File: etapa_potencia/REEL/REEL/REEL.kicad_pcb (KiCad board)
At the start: 2 copper layers, 30 parts, among them J1 USB_B_Mini, SW1 SW_Push, SW2 SW_Reed, SW3 SW_Push, U1 Tp5400, U2 ESP32-WROOM-32, U3 FT232, U4 AMS1117-3.3

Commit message: Adición etapa de audio
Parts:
- D3: value SMBJ5383B -> DIOM4336X265N
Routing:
- net GND: track 0.00 -> 295.5 mm
- net +5V: track 0.00 -> 166.8 mm
- net Net-(D1-Pad2): track 0.00 -> 107.7 mm, vias 0 -> 2
- net /RESET: track 0.00 -> 98.7 mm, vias 0 -> 2
- net Net-(R7-Pad1): track 0.00 -> 97.5 mm, vias 0 -> 1
- net /GPIO0: track 0.00 -> 85.4 mm, vias 0 -> 2
- net Net-(D1-Pad1): track 0.00 -> 85.1 mm, vias 0 -> 2
- net +3V3: track 0.00 -> 84.8 mm, vias 0 -> 2
- net Net-(SW2-Pad2): track 0.00 -> 69.8 mm, vias 0 -> 1
- net Net-(D2-Pad1): track 0.00 -> 22.7 mm
- net Net-(R5-Pad1): track 0.00 -> 17.8 mm, vias 0 -> 2

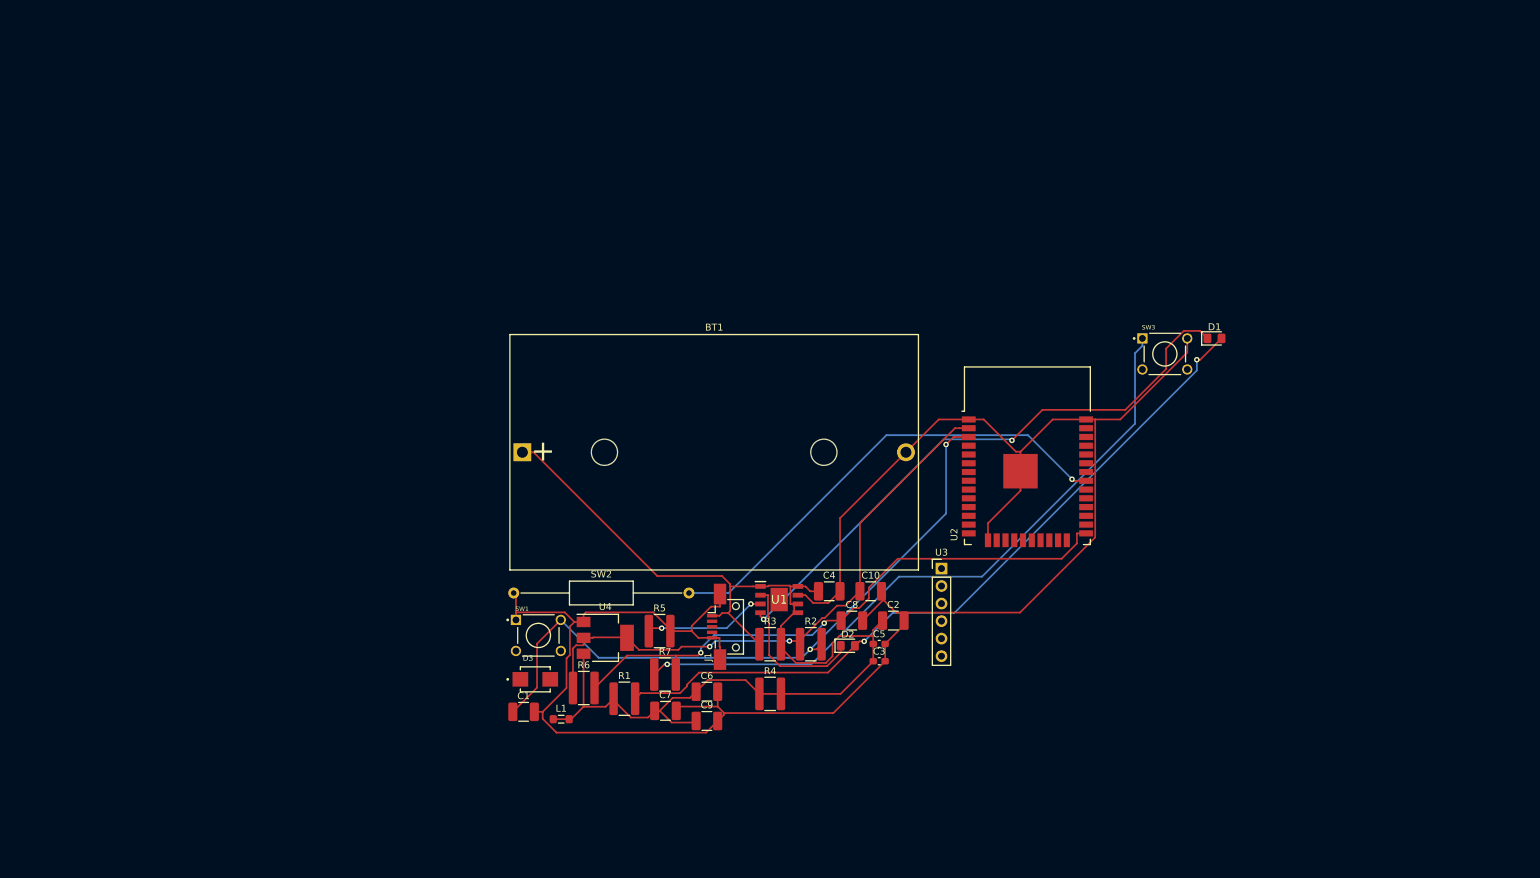
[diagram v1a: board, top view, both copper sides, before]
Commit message: Conexiones corregidas, PCB ordenada
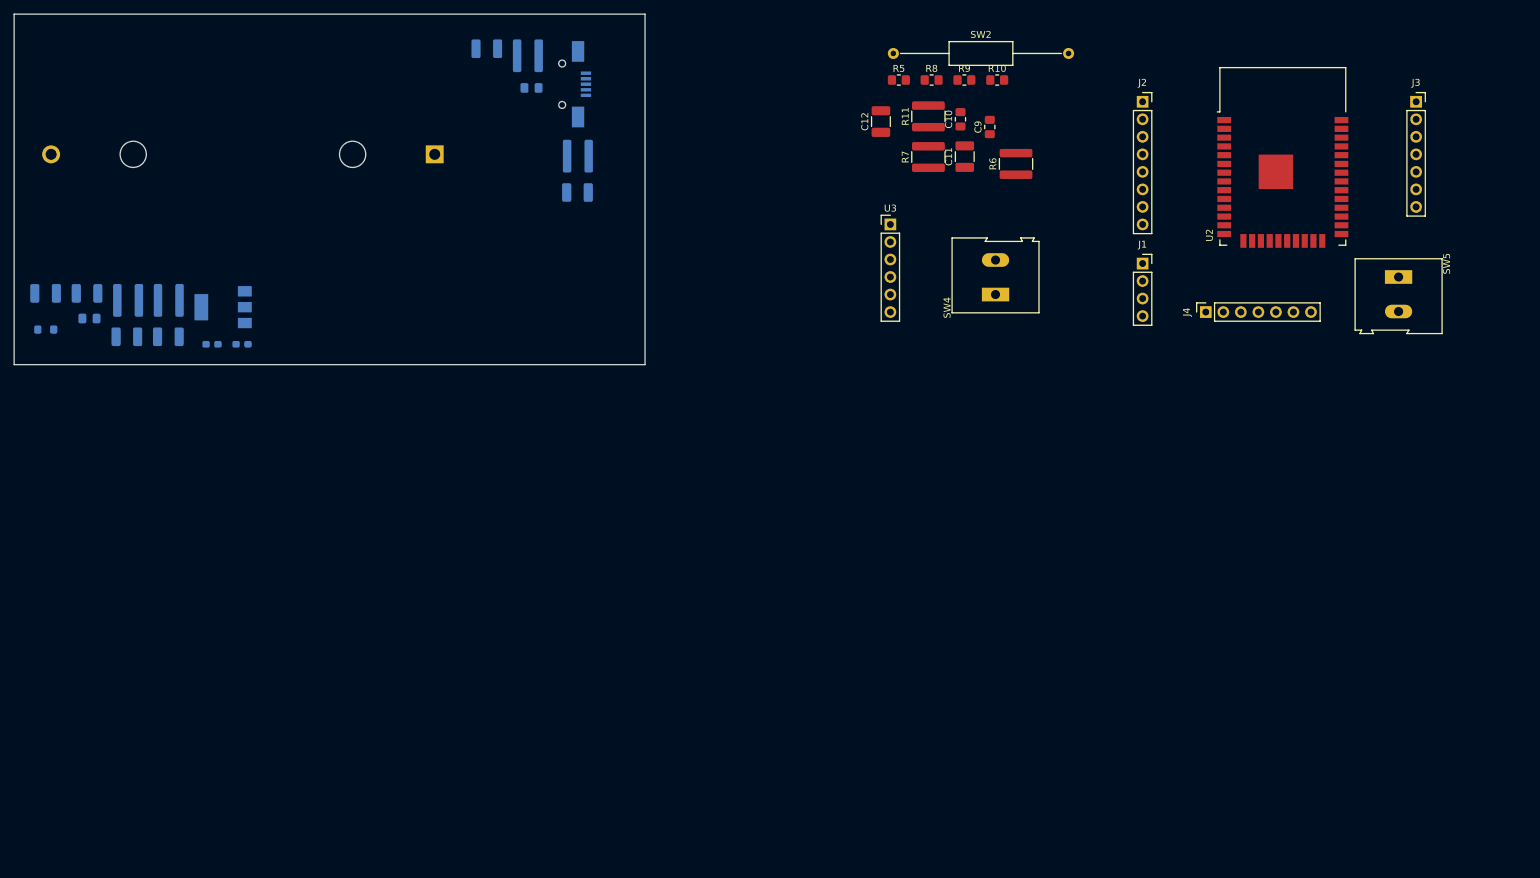
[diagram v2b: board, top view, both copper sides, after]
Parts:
- removed D3: DIOM4336X265N, SMBJ5383B:SMBJ5383B
- removed SW1, SW3: SW_Push, Button_1825910-6:SW_1825910-6-4
- removed U1: Tp5400, KiCad:TP5410
- added C11: 100n, Capacitor_SMD:C_1210_3225Metric_Pad1.33x2.70mm_HandSolder, F.Cu at (155.6, 38.4)
- added C12: 100n, Capacitor_SMD:C_1210_3225Metric_Pad1.33x2.70mm_HandSolder, F.Cu at (143.4, 33.4)
- added J2: Conn_display_2, Connector_PinSocket_2.54mm:PinSocket_1x08_P2.54mm_Vertical, F.Cu at (181.3, 30.5)
- added J3: Conn_teclado, Connector_PinSocket_2.54mm:PinSocket_1x07_P2.54mm_Vertical, F.Cu at (221.0, 30.5)
- added J4: Conn_audio, Connector_PinSocket_2.54mm:PinSocket_1x07_P2.54mm_Vertical, F.Cu at (190.5, 61.0)
- added J5: USB_B_Mini, Connector_USB:USB_Mini-B_AdamTech_MUSB-B5-S-VT-TSMT-1_SMD_Vertical, B.Cu at (99.1, 27.9)
- added R10: 5.1k, Resistor_SMD:R_0805_2012Metric_Pad1.20x1.40mm_HandSolder, F.Cu at (160.3, 27.3)
- added R11: 10k, Resistor_SMD:R_1218_3246Metric_Pad1.22x4.75mm_HandSolder, F.Cu at (150.3, 32.6)
- added R8: 5.1k, Resistor_SMD:R_0805_2012Metric_Pad1.20x1.40mm_HandSolder, F.Cu at (150.8, 27.3)
- added R9: 51k, Resistor_SMD:R_0805_2012Metric_Pad1.20x1.40mm_HandSolder, F.Cu at (155.5, 27.3)
- added SW4: BW, TerminalBlock:TerminalBlock_Altech_AK300-2_P5.00mm, F.Cu at (160.0, 58.4)
- added SW5: FW, TerminalBlock:TerminalBlock_Altech_AK300-2_P5.00mm, F.Cu at (218.4, 55.9)
- BT1, C6, D1, D2, L1, U4: moved to B.Cu
- C1, C8: value 100n -> 10u; moved to B.Cu
- C10, C9: value 10u -> 100n; footprint Capacitor_SMD:C_1210_3225Metric_Pad1.33x2.70mm_HandSolder -> Capacitor_SMD:C_0805_2012Metric_Pad1.18x1.45mm_HandSolder
- C2: value 10u -> 0.1u; footprint Capacitor_SMD:C_1210_3225Metric_Pad1.33x2.70mm_HandSolder -> Capacitor_SMD:C_0603_1608Metric_Pad1.08x0.95mm_HandSolder; moved to B.Cu
- C3: value 0.1u -> 47u; footprint Capacitor_SMD:C_0603_1608Metric_Pad1.08x0.95mm_HandSolder -> Capacitor_SMD:C_1210_3225Metric_Pad1.33x2.70mm_HandSolder; moved to B.Cu
- C4: value 22u -> 0.1u; footprint Capacitor_SMD:C_1210_3225Metric_Pad1.33x2.70mm_HandSolder -> Capacitor_SMD:C_0603_1608Metric_Pad1.08x0.95mm_HandSolder; moved to B.Cu
- C5: value 0.1u -> 22u; footprint Capacitor_SMD:C_0603_1608Metric_Pad1.08x0.95mm_HandSolder -> Capacitor_SMD:C_1210_3225Metric_Pad1.33x2.70mm_HandSolder; moved to B.Cu
- C7: value 47u -> 10u; moved to B.Cu
- J1: value USB_B_Mini -> Conn_display2; footprint Connector_USB:USB_Mini-B_AdamTech_MUSB-B5-S-VT-TSMT-1_SMD_Vertical -> Connector_PinSocket_2.54mm:PinSocket_1x04_P2.54mm_Vertical
- R1: value 1k -> 1; moved to B.Cu
- R2: value 10k -> 1; moved to B.Cu
- R3: value 1 -> 1k; moved to B.Cu
- R4: value 1 -> 1.1k; moved to B.Cu
- R5: value 1.1k -> 51k; footprint Resistor_SMD:R_1218_3246Metric_Pad1.22x4.75mm_HandSolder -> Resistor_SMD:R_0805_2012Metric_Pad1.20x1.40mm_HandSolder
- moved D1 163.1 mm to (28.7, 61.9), turned to 180 degrees
- moved C5 131.1 mm to (22.3, 58.2), turned to 180 degrees
- moved C8 120.6 mm to (28.3, 58.2), turned to 180 degrees
- moved C2 106.6 mm to (46.5, 65.6), turned to 180 degrees
- moved R2 105.6 mm to (40.2, 59.3), turned to 180 degrees
- moved R3 105.6 mm to (34.3, 59.3), turned to 180 degrees
- moved C3 105.4 mm to (86.3, 22.8), turned to 180 degrees
- moved C6 98.6 mm to (34.1, 64.5), turned to 180 degrees
- moved R6 98.5 mm to (163.0, 39.5), turned to 90 degrees
- moved SW2 95.6 mm to (145.2, 23.5)
- moved C9 95.4 mm to (159.2, 34.1), turned to 90 degrees
- moved R1 94.2 mm to (92.2, 23.8), turned to 180 degrees
- moved L1 93.7 mm to (22.4, 63.5), turned to 180 degrees
- moved D2 92.9 mm to (92.8, 28.5), turned to 180 degrees
- moved C4 92.3 mm to (50.8, 65.6), turned to 180 degrees
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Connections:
- net TX_D0 renamed /TX_D0
- C1 pad 1: /RESET -> +5V
- C10 pad 1: +3V3 -> GND
- C10 pad 2: GND -> /FW
- C8 pad 1: /GPIO0 -> +3V3
- C9 pad 1: +5V -> GND
- C9 pad 2: GND -> /BW
- J1 pad 1: +5V -> /IO33
- J1 pad 2: /D- -> /MOSI
- J1 pad 3: /D+ -> /IO32
- J1 pad 4: unconnected-(J1-Pad4) -> /SCK
- R1 pad 2: Net-(D1-Pad2) -> +5V
- R2 pad 1: +3V3 -> +5V
- R2 pad 2: /RESET -> +5V
- R3 pad 2: +5V -> Net-(D1-Pad2)
- R4 pad 1: +5V -> Net-(R4-Pad1)
- R4 pad 2: +5V -> GND
- R5 pad 1: Net-(R5-Pad1) -> /BW
- R5 pad 2: GND -> +3V3
- R6 pad 2: /GPIO0 -> /IO0
- R7 pad 2: /GPIO0 -> /IO0
- SW2 pad 2: Net-(SW2-Pad2) -> Net-(U2-Pad16)
- U2 pad 10: unconnected-(U2-Pad10) -> /CS
- U2 pad 11: unconnected-(U2-Pad11) -> /IO33
- U2 pad 12: unconnected-(U2-Pad12) -> /IO32
- U2 pad 13: unconnected-(U2-Pad13) -> /BW
- U2 pad 16: unconnected-(U2-Pad16) -> Net-(U2-Pad16)
- U2 pad 23: unconnected-(U2-Pad23) -> /IO0
- U2 pad 25: /GPIO0 -> /I2S_DIN
- U2 pad 26: unconnected-(U2-Pad26) -> /I2S_CLK
- U2 pad 27: unconnected-(U2-Pad27) -> /I2S_WS
- U2 pad 28: unconnected-(U2-Pad28) -> /IO27
- U2 pad 29: unconnected-(U2-Pad29) -> /IO26
- U2 pad 3: /RESET -> /EN
- U2 pad 30: unconnected-(U2-Pad30) -> /IO25
- U2 pad 31: Net-(SW2-Pad2) -> /IO17
- U2 pad 33: unconnected-(U2-Pad33) -> /IO14
- U2 pad 34: RX_D0 -> /IO13
- U2 pad 36: unconnected-(U2-Pad36) -> /RX_D0
- U2 pad 37: unconnected-(U2-Pad37) -> /FW
- U2 pad 6: unconnected-(U2-Pad6) -> /SCK
- U2 pad 7: unconnected-(U2-Pad7) -> /MOSI
- U2 pad 8: unconnected-(U2-Pad8) -> /D/C
- U2 pad 9: unconnected-(U2-Pad9) -> /Rst_d
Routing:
- net GND: track 295.5 -> 0.00 mm
- net +5V: track 166.8 -> 0.00 mm
- net Net-(D1-Pad2): track 107.7 -> 0.00 mm, vias 2 -> 0
- net /RESET: track 98.7 -> 0.00 mm, vias 2 -> 0
- net Net-(R7-Pad1): track 97.5 -> 0.00 mm, vias 1 -> 0
- net /GPIO0: track 85.4 -> 0.00 mm, vias 2 -> 0
- net Net-(D1-Pad1): track 85.1 -> 0.00 mm, vias 2 -> 0
- net +3V3: track 84.8 -> 0.00 mm, vias 2 -> 0
- net Net-(SW2-Pad2): track 69.8 -> 0.00 mm, vias 1 -> 0
- net Net-(D2-Pad1): track 22.7 -> 0.00 mm
- net Net-(R5-Pad1): track 17.8 -> 0.00 mm, vias 2 -> 0
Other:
- board outline added: 91.4 x 50.8 mm
- board text added: "Parte posterior"
- board text added: "Parte superior"

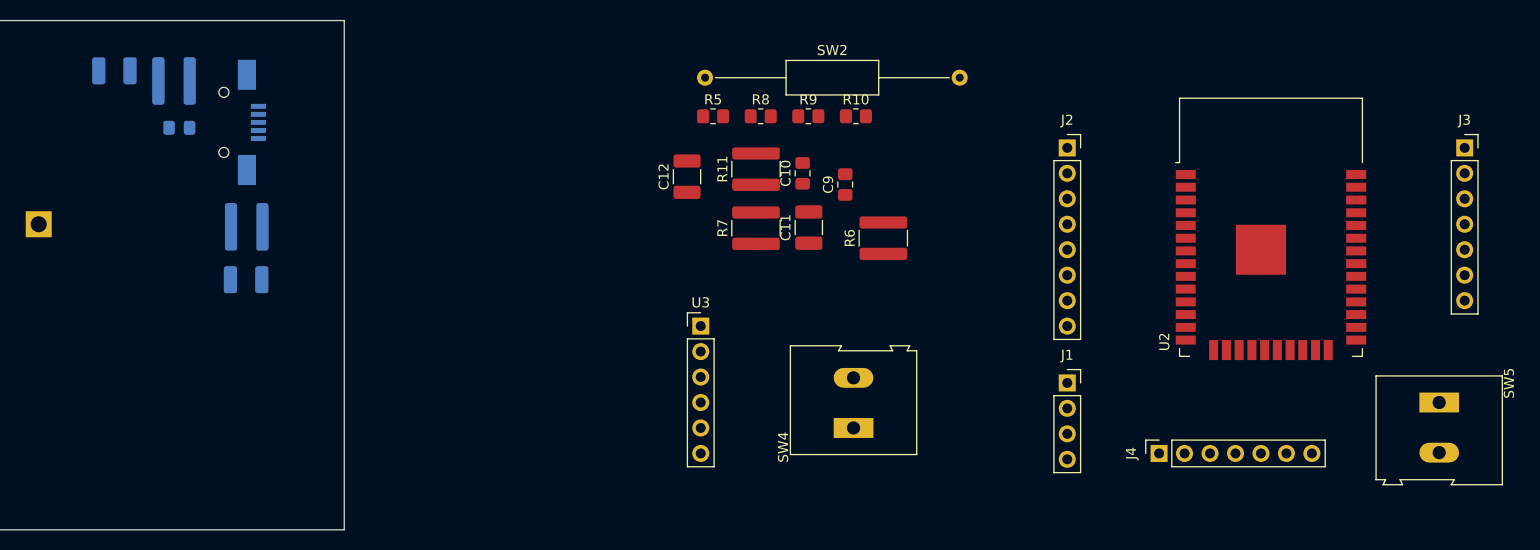
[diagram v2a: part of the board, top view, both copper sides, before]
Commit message: adicion matriz vias
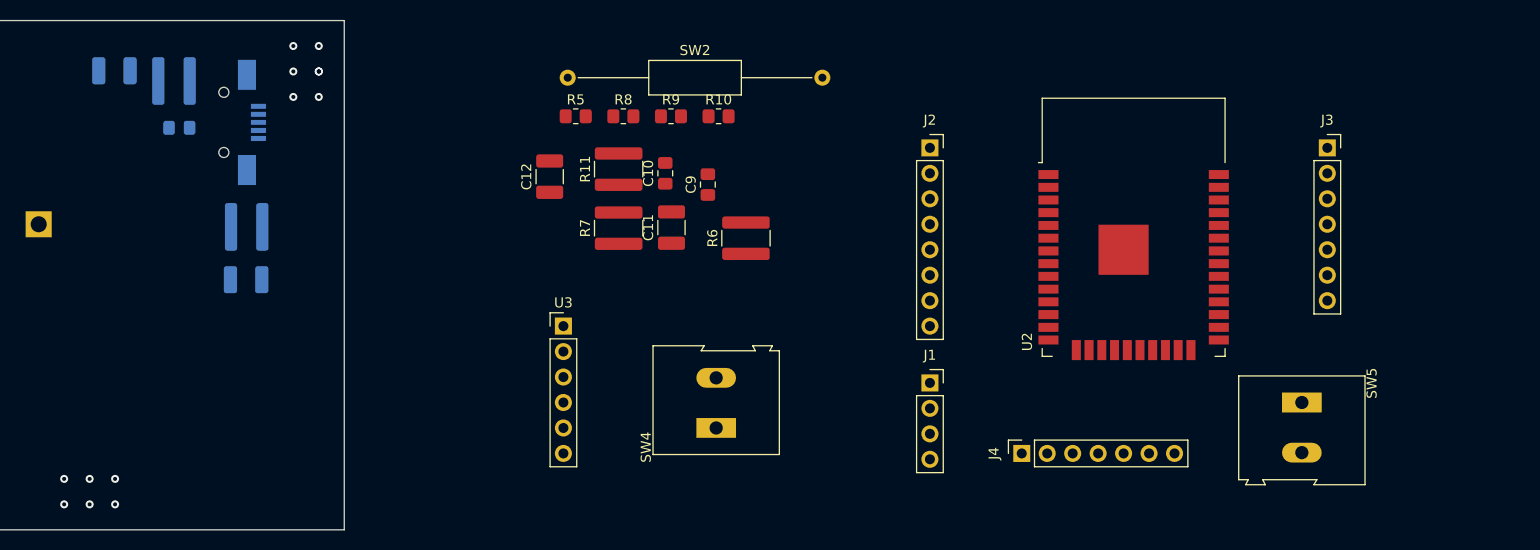
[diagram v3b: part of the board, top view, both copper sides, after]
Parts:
- moved J1 13.7 mm to (167.6, 53.9)
- moved J2 13.7 mm to (167.6, 30.5)
- moved R6 13.7 mm to (149.3, 39.5)
- moved SW2 13.7 mm to (131.5, 23.5)
- moved SW4 13.7 mm to (146.3, 58.4)
- moved C10 13.7 mm to (141.2, 33.0)
- moved C11 13.7 mm to (141.9, 38.4)
- moved C12 13.7 mm to (129.7, 33.4)
- moved C9 13.7 mm to (145.5, 34.1)
- moved J3 13.7 mm to (207.3, 30.5)
- moved J4 13.7 mm to (176.8, 61.0)
- moved R10 13.7 mm to (146.6, 27.3)
- moved R11 13.7 mm to (136.6, 32.6)
- moved R5 13.7 mm to (132.3, 27.3)
- moved R7 13.7 mm to (136.6, 38.5)
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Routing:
- net (no net): vias 0 -> 13

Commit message: Primera organización huellas
Organización de huellas y conectores, falta parte de potencia
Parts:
- added SW1: SW_Push, TerminalBlock:TerminalBlock_Altech_AK300-2_P5.00mm, F.Cu at (157.5, 40.6)
- C11, C12: footprint Capacitor_SMD:C_1210_3225Metric_Pad1.33x2.70mm_HandSolder -> Capacitor_SMD:C_0805_2012Metric_Pad1.18x1.45mm_HandSolder
- R11, R6: footprint Resistor_SMD:R_1218_3246Metric_Pad1.22x4.75mm_HandSolder -> Resistor_SMD:R_0805_2012Metric_Pad1.20x1.40mm_HandSolder
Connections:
- net /IO17 renamed /T4
- net /IO25 renamed /T5
- net /IO26 renamed /T6
- net /IO27 renamed /T7
- net /IO33 renamed /SDCS
- C12 pad 1: /IO0 -> /Prom
- J1 pad 3: /IO32 -> /SDMISO
- J3 pad 1: /IO13 -> /T1
- J3 pad 2: /IO14 -> /T2
- J3 pad 3: /IO16 -> /T3
- R6 pad 2: /IO0 -> /Prom
- R7 pad 2: /IO0 -> /Prom
- U2 pad 12: /IO32 -> /T2
- U2 pad 14: unconnected-(U2-Pad14) -> /T3
- U2 pad 23: /IO0 -> /I2S_DIN
- U2 pad 25: /I2S_DIN -> /Prom
- U2 pad 33: /IO14 -> /SDMISO
- U2 pad 34: /IO13 -> /RX_D0
- U2 pad 36: /RX_D0 -> /T1
